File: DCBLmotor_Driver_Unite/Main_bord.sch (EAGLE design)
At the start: 50 parts, among them CN1 DF11-16DP-2DSA, CN2 DF11-16DP-2DSA, CN3 DF11-4DS-2C, CN4 HIF3FC-10PA-2.54DSA(71), CN5 HIF3FC-10PA-2.54DSA(71), IC1 TMPM370FYFG, IC2 MCP2561FD-E/MF, IC3 AM26C32CD, IC4 AM26C32CD, SW1 CVS-02TB

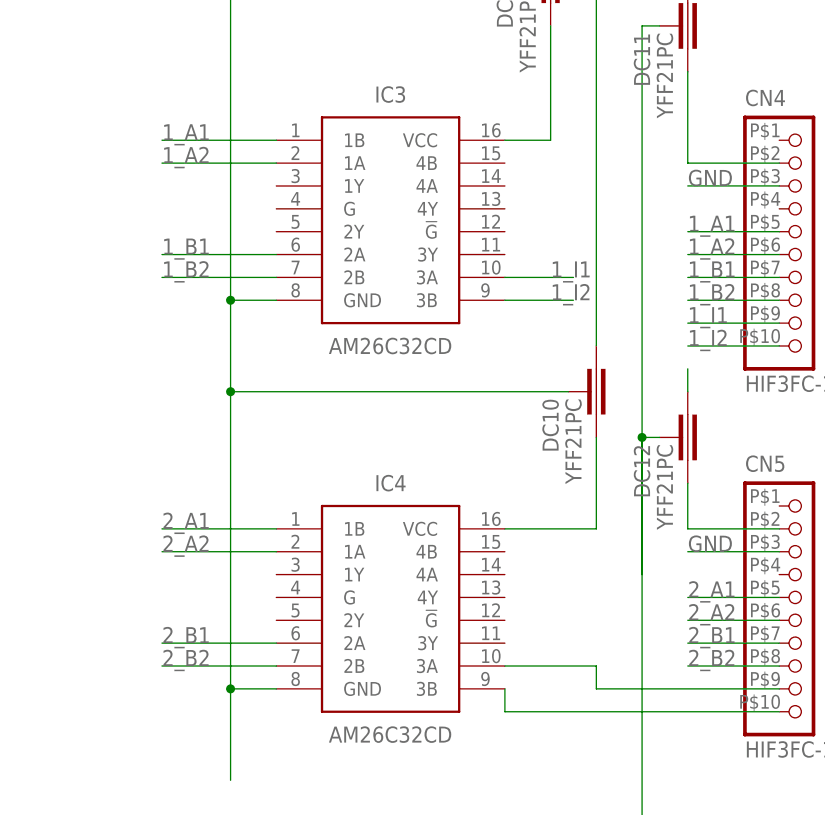
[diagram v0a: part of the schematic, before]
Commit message: Mount Endcoder
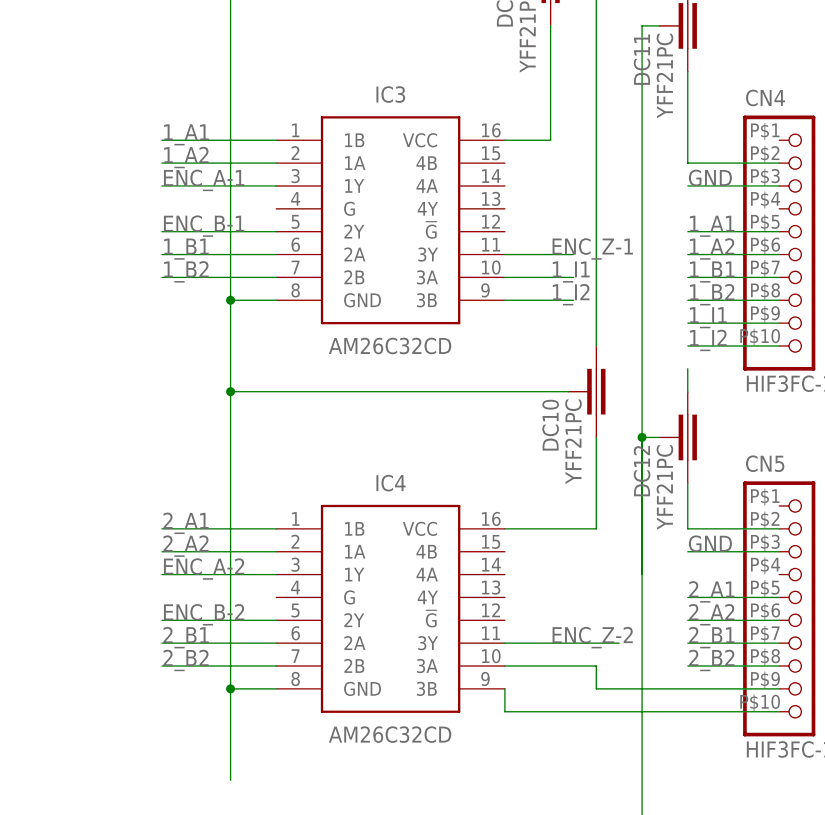
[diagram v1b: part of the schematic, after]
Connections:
- net ENC_A-1: now also IC3.1Y
- net ENC_A-2: now also IC4.1Y
- net ENC_B-1: now also IC3.2Y
- net ENC_B-2: now also IC4.2Y
- net ENC_Z-1: now also IC3.3Y
- net ENC_Z-2: now also IC4.3Y
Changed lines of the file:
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@@
 <label x="38.1" y="-20.32" size="1.778" layer="95" rot="R90"/>
+</segment>
+<segment>
+<wire x1="-83.82" y1="-53.34" x2="-91.44" y2="-53.34" width="0.1524" layer="91"/>
+<label x="-86.36" y="-53.34" size="1.778" layer="95"/>
+<pinref part="IC3" gate="G$1" pin="3Y"/>
 </segment>
 </net>
@@
 <label x="114.3" y="17.78" size="1.778" layer="95"/>
 </segment>
+<segment>
+<wire x1="-129.54" y1="-88.9" x2="-116.84" y2="-88.9" width="0.1524" layer="91"/>
+<label x="-129.54" y="-88.9" size="1.778" layer="95"/>
+<pinref part="IC4" gate="G$1" pin="1Y"/>
+</segment>
 </net>
 <net name="ENC_B-2" class="0">
@@
 <wire x1="111.76" y1="20.32" x2="121.92" y2="20.32" width="0.1524" layer="91"/>
 <label x="114.3" y="20.32" size="1.778" layer="95"/>
+</segment>
+<segment>
+<wire x1="-129.54" y1="-93.98" x2="-116.84" y2="-93.98" width="0.1524" layer="91"/>
+<label x="-129.54" y="-93.98" size="1.778" layer="95"/>
+<pinref part="IC4" gate="G$1" pin="2Y"/>
 </segment>
 </net>
@@
 <label x="114.3" y="22.86" size="1.778" layer="95"/>
 </segment>
+<segment>
+<wire x1="-91.44" y1="-96.52" x2="-78.74" y2="-96.52" width="0.1524" layer="91"/>
+<label x="-86.36" y="-96.52" size="1.778" layer="95"/>
+<pinref part="IC4" gate="G$1" pin="3Y"/>
+</segment>
 </net>
 <net name="ENC_B-1" class="0">
@@
 <wire x1="35.56" y1="-7.62" x2="35.56" y2="-20.32" width="0.1524" layer="91"/>
 <label x="35.56" y="-20.32" size="1.778" layer="95" rot="R90"/>
+</segment>
+<segment>
+<wire x1="-116.84" y1="-50.8" x2="-129.54" y2="-50.8" width="0.1524" layer="91"/>
+<label x="-129.54" y="-50.8" size="1.778" layer="95"/>
+<pinref part="IC3" gate="G$1" pin="2Y"/>
 </segment>
 </net>
@@
 <label x="33.02" y="-20.32" size="1.778" layer="95" rot="R90"/>
 </segment>
+<segment>
+<wire x1="-116.84" y1="-45.72" x2="-129.54" y2="-45.72" width="0.1524" layer="91"/>
+<label x="-129.54" y="-45.72" size="1.778" layer="95"/>
+<pinref part="IC3" gate="G$1" pin="1Y"/>
+</segment>
 </net>

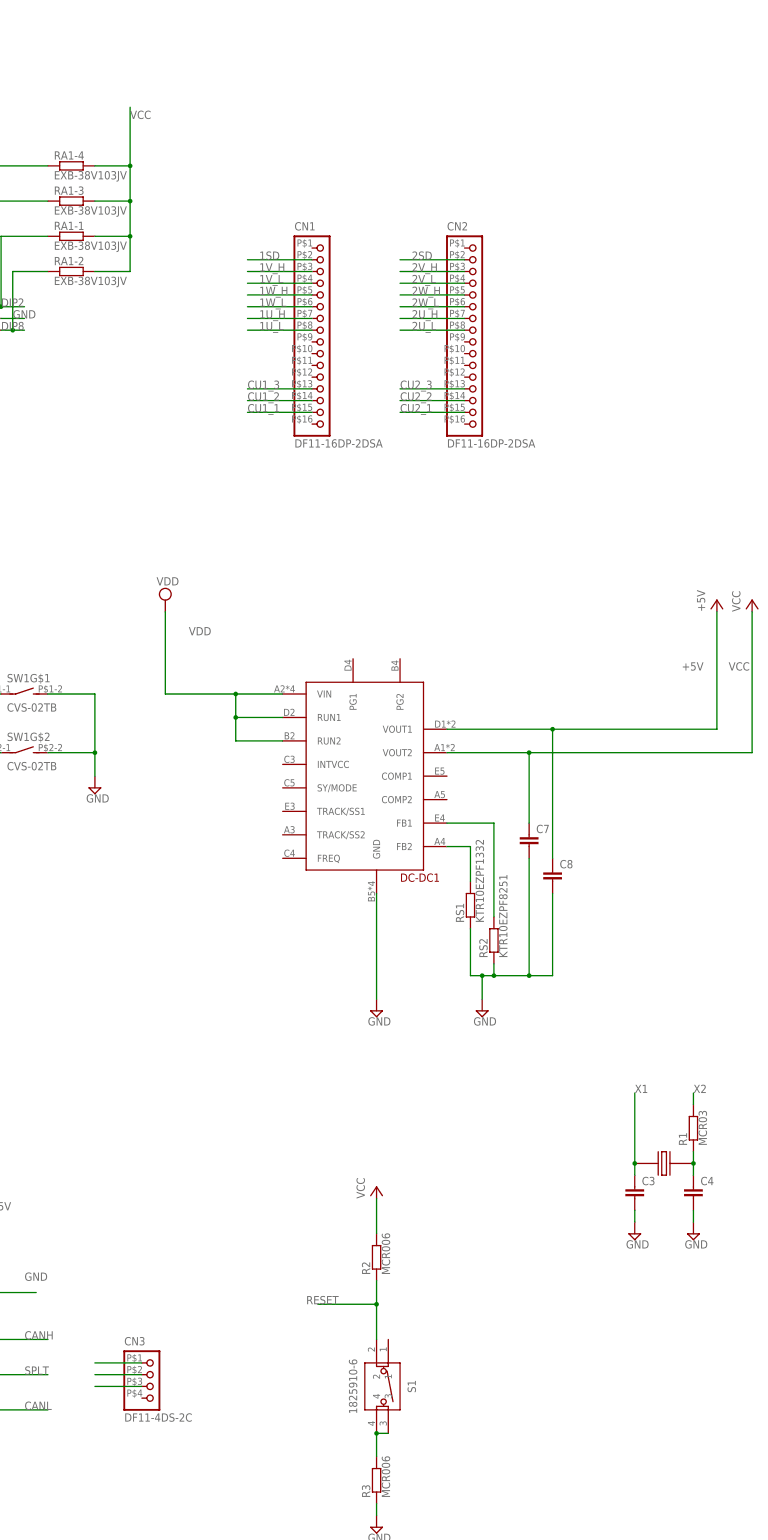
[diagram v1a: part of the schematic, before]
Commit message: Mount new parts
mount 
holl conecter
change
reset switch
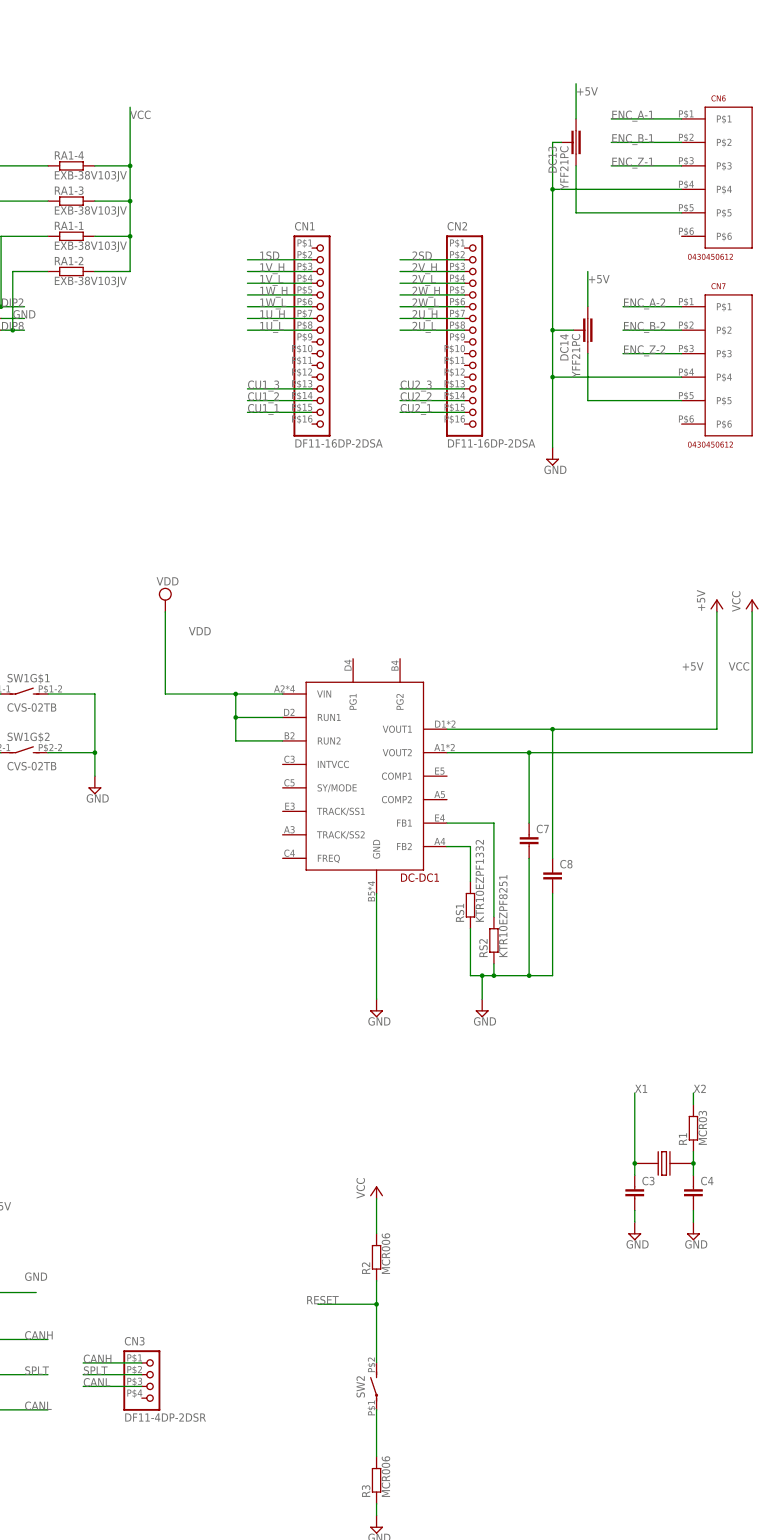
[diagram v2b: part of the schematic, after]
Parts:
- removed S1: 1825910-6, 1825910-6:1825910-6
- added CN6, CN7: 0430450612, Molex:0430450612
- added DC13, DC14: YFF21PC, TDK:YFF21PC
- added SW2: EVQ-PE104K, Panasonic:EVQ-PE104K
- CN3: value DF11-4DS-2C -> DF11-4DP-2DSR; device Hirose:DF11-4DS-2C -> Hirose:DF11-4DP-2DSR
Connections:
- new net N$32: CN6.P$5, DC13.P$2
- new net N$33: CN7.P$5, DC14.P$2
- net +5V: now also DC13.P$1, DC14.P$1
- net ENC_A-1: now also CN6.P$1
- net ENC_A-2: now also CN7.P$1
- net ENC_B-1: now also CN6.P$2
- net ENC_B-2: now also CN7.P$2
- net ENC_Z-1: now also CN6.P$3
- net ENC_Z-2: now also CN7.P$3
- net GND: now also CN6.P$4, CN7.P$4, DC13.GND, DC14.GND
- net N$12: now also SW2.P; no longer S1.3, S1.4
- net RESET: now also SW2.S; no longer S1.2
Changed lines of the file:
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@@
 <part name="R3" library="ROHM" deviceset="MCR006" device=""/>
 <part name="SUPPLY15" library="supply2" library_urn="urn:adsk.eagle:library:372" deviceset="GND" device=""/>
-<part name="S1" library="1825910-6" deviceset="1825910-6" device=""/>
 <part name="P+2" library="supply1" library_urn="urn:adsk.eagle:library:371" deviceset="VCC" device="" value="+5V"/>
 <part name="P+3" library="supply1" library_urn="urn:adsk.eagle:library:371" deviceset="VCC" device="" value="+5V"/>
@@
 <part name="R4" library="ROHM" deviceset="MCR006" device=""/>
 <part name="R5" library="ROHM" deviceset="MCR006" device=""/>
-<part name="CN3" library="Hirose" deviceset="DF11-4DS-2C" device=""/>
+<part name="CN3" library="Hirose" deviceset="DF11-4DP-2DSR" device=""/>
 <part name="S2" library="220AMA16R" deviceset="220AMA16R" device=""/>
 <part name="SW1" library="Nidec" deviceset="CVS-02TB" device=""/>
@@
 <part name="DC11" library="TDK" deviceset="YFF21PC" device=""/>
 <part name="DC12" library="TDK" deviceset="YFF21PC" device=""/>
+<part name="SW2" library="Panasonic" deviceset="EVQ-PE104K" device=""/>
+<part name="CN6" library="Molex" deviceset="0430450612" device=""/>
+<part name="CN7" library="Molex" deviceset="0430450612" device=""/>
+<part name="DC13" library="TDK" deviceset="YFF21PC" device=""/>
+<part name="DC14" library="TDK" deviceset="YFF21PC" device=""/>
+<part name="SUPPLY17" library="supply2" library_urn="urn:adsk.eagle:library:372" deviceset="GND" device=""/>
 </parts>
 <sheets>
@@
 <instance part="R3" gate="G$1" x="393.7" y="-119.38" rot="R90"/>
 <instance part="SUPPLY15" gate="GND" x="393.7" y="-129.54"/>
-<instance part="S1" gate="G$1" x="396.24" y="-88.9" rot="R270"/>
 <instance part="P+2" gate="VCC" x="246.38" y="81.28"/>
 <instance part="P+3" gate="VCC" x="231.14" y="81.28"/>
@@
 <instance part="DC11" gate="G$1" x="-71.12" y="-27.94" rot="R270"/>
 <instance part="DC12" gate="G$1" x="-71.12" y="-73.66" rot="R270"/>
+<instance part="SW2" gate="G$1" x="393.7" y="-99.06"/>
+<instance part="CN6" gate="G$1" x="464.82" y="165.1"/>
+<instance part="CN7" gate="G$1" x="464.82" y="124.46"/>
+<instance part="DC13" gate="G$1" x="436.88" y="170.18" rot="R270"/>
+<instance part="DC14" gate="G$1" x="439.42" y="129.54" rot="R270"/>
+<instance part="SUPPLY17" gate="GND" x="431.8" y="101.6"/>
 </instances>
 <busses>
@@
 <wire x1="-76.2" y1="-73.66" x2="-76.2" y2="-116.84" width="0.1524" layer="91"/>
 </segment>
+<segment>
+<pinref part="DC13" gate="G$1" pin="GND"/>
+<wire x1="433.76" y1="170.18" x2="431.8" y2="170.18" width="0.1524" layer="91"/>
+<wire x1="431.8" y1="170.18" x2="431.8" y2="160.02" width="0.1524" layer="91"/>
+<pinref part="DC14" gate="G$1" pin="GND"/>
+<wire x1="431.8" y1="160.02" x2="431.8" y2="129.54" width="0.1524" layer="91"/>
+<wire x1="431.8" y1="129.54" x2="431.8" y2="119.38" width="0.1524" layer="91"/>
+<wire x1="431.8" y1="119.38" x2="431.8" y2="104.14" width="0.1524" layer="91"/>
+<wire x1="436.3" y1="129.54" x2="431.8" y2="129.54" width="0.1524" layer="91"/>
+<junction x="431.8" y="129.54"/>
+<pinref part="CN7" gate="G$1" pin="P$4"/>
+<wire x1="459.74" y1="119.38" x2="431.8" y2="119.38" width="0.1524" layer="91"/>
+<junction x="431.8" y="119.38"/>
+<pinref part="CN6" gate="G$1" pin="P$4"/>
+<wire x1="459.74" y1="160.02" x2="431.8" y2="160.02" width="0.1524" layer="91"/>
+<junction x="431.8" y="160.02"/>
+<pinref part="SUPPLY17" gate="GND" pin="GND"/>
+</segment>
 </net>
 <net name="N$7" class="0">
@@
 <wire x1="-71.12" y1="-68.58" x2="-71.12" y2="-66.04" width="0.1524" layer="91"/>
 </segment>
+<segment>
+<pinref part="DC13" gate="G$1" pin="P$1"/>
+<wire x1="436.88" y1="175.26" x2="436.88" y2="182.88" width="0.1524" layer="91"/>
+<label x="436.88" y="180.34" size="1.778" layer="95"/>
+</segment>
+<segment>
+<pinref part="DC14" gate="G$1" pin="P$1"/>
+<wire x1="439.42" y1="134.62" x2="439.42" y2="142.24" width="0.1524" layer="91"/>
+<label x="439.42" y="139.7" size="1.778" layer="95"/>
+</segment>
 </net>
 <net name="VDD" class="0">
@@
 <junction x="393.7" y="-81.28"/>
 <label x="378.46" y="-81.28" size="1.778" layer="95"/>
-<pinref part="S1" gate="G$1" pin="2"/>
-<wire x1="393.7" y1="-88.9" x2="393.7" y2="-81.28" width="0.1524" layer="91"/>
+<wire x1="393.7" y1="-93.98" x2="393.7" y2="-81.28" width="0.1524" layer="91"/>
+<pinref part="SW2" gate="G$1" pin="S"/>
 </segment>
 </net>
@@
 <segment>
 <pinref part="R3" gate="G$1" pin="1"/>
-<pinref part="S1" gate="G$1" pin="4"/>
-<wire x1="393.7" y1="-114.3" x2="393.7" y2="-109.22" width="0.1524" layer="91"/>
-<pinref part="S1" gate="G$1" pin="3"/>
-<wire x1="393.7" y1="-109.22" x2="396.24" y2="-109.22" width="0.1524" layer="91"/>
-<junction x="393.7" y="-109.22"/>
+<pinref part="SW2" gate="G$1" pin="P"/>
+<wire x1="393.7" y1="-104.14" x2="393.7" y2="-114.3" width="0.1524" layer="91"/>
 </segment>
 </net>
@@
 <pinref part="IC3" gate="G$1" pin="3Y"/>
 </segment>
+<segment>
+<wire x1="459.74" y1="165.1" x2="444.5" y2="165.1" width="0.1524" layer="91"/>
+<label x="444.5" y="165.1" size="1.778" layer="95"/>
+<pinref part="CN6" gate="G$1" pin="P$3"/>
+</segment>
 </net>
 <net name="ENC_A-2" class="0">
@@
 <pinref part="IC4" gate="G$1" pin="1Y"/>
 </segment>
+<segment>
+<wire x1="447.04" y1="134.62" x2="459.74" y2="134.62" width="0.1524" layer="91"/>
+<label x="447.04" y="134.62" size="1.778" layer="95"/>
+<pinref part="CN7" gate="G$1" pin="P$1"/>
+</segment>
 </net>
 <net name="ENC_B-2" class="0">
@@
 <pinref part="IC4" gate="G$1" pin="2Y"/>
 </segment>
+<segment>
+<wire x1="447.04" y1="129.54" x2="459.74" y2="129.54" width="0.1524" layer="91"/>
+<label x="447.04" y="129.54" size="1.778" layer="95"/>
+<pinref part="CN7" gate="G$1" pin="P$2"/>
+</segment>
 </net>
 <net name="ENC_Z-2" class="0">
@@
 <pinref part="IC4" gate="G$1" pin="3Y"/>
 </segment>
+<segment>
+<wire x1="447.04" y1="124.46" x2="459.74" y2="124.46" width="0.1524" layer="91"/>
+<label x="447.04" y="124.46" size="1.778" layer="95"/>
+<pinref part="CN7" gate="G$1" pin="P$3"/>
+</segment>
 </net>
 <net name="ENC_B-1" class="0">
@@
 <pinref part="IC3" gate="G$1" pin="2Y"/>
 </segment>
+<segment>
+<wire x1="459.74" y1="170.18" x2="444.5" y2="170.18" width="0.1524" layer="91"/>
+<label x="444.5" y="170.18" size="1.778" layer="95"/>
+<pinref part="CN6" gate="G$1" pin="P$2"/>
+</segment>
 </net>
 <net name="ENC_A-1" class="0">
@@
 <label x="-129.54" y="-45.72" size="1.778" layer="95"/>
 <pinref part="IC3" gate="G$1" pin="1Y"/>
+</segment>
+<segment>
+<wire x1="459.74" y1="175.26" x2="444.5" y2="175.26" width="0.1524" layer="91"/>
+<label x="444.5" y="175.26" size="1.778" layer="95"/>
+<pinref part="CN6" gate="G$1" pin="P$1"/>
 </segment>
 </net>
@@
 <segment>
 <pinref part="CN3" gate="G$1" pin="1"/>
-<wire x1="342.9" y1="-93.98" x2="332.74" y2="-93.98" width="0.1524" layer="91"/>
+<wire x1="342.9" y1="-93.98" x2="330.2" y2="-93.98" width="0.1524" layer="91"/>
+<label x="330.2" y="-93.98" size="1.778" layer="95"/>
 </segment>
 </net>
@@
 <segment>
 <pinref part="CN3" gate="G$1" pin="3"/>
-<wire x1="342.9" y1="-99.06" x2="332.74" y2="-99.06" width="0.1524" layer="91"/>
+<wire x1="342.9" y1="-99.06" x2="330.2" y2="-99.06" width="0.1524" layer="91"/>
+<label x="330.2" y="-99.06" size="1.778" layer="95"/>
 </segment>
 </net>
@@
 <segment>
 <pinref part="CN3" gate="G$1" pin="2"/>
-<wire x1="342.9" y1="-96.52" x2="332.74" y2="-96.52" width="0.1524" layer="91"/>
+<wire x1="342.9" y1="-96.52" x2="330.2" y2="-96.52" width="0.1524" layer="91"/>
+<label x="330.2" y="-96.52" size="1.778" layer="95"/>
 </segment>
 </net>
@@
 </segment>
 </net>
+<net name="N$32" class="0">
+<segment>
+<pinref part="DC13" gate="G$1" pin="P$2"/>
+<pinref part="CN6" gate="G$1" pin="P$5"/>
+<wire x1="436.88" y1="165.1" x2="436.88" y2="154.94" width="0.1524" layer="91"/>
+<wire x1="436.88" y1="154.94" x2="459.74" y2="154.94" width="0.1524" layer="91"/>
+</segment>
+</net>
+<net name="N$33" class="0">
+<segment>
+<pinref part="DC14" gate="G$1" pin="P$2"/>
+<pinref part="CN7" gate="G$1" pin="P$5"/>
+<wire x1="439.42" y1="124.46" x2="439.42" y2="114.3" width="0.1524" layer="91"/>
+<wire x1="439.42" y1="114.3" x2="459.74" y2="114.3" width="0.1524" layer="91"/>
+</segment>
+</net>

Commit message: Version1 per finshed
Per complete Version1
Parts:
- added 0R1, 0R2: 5106, Keystone:5106
- added C5: T356L107K016AT, KEMET:T356L107K016AT
- added CN10: (no value), jst-xh:B2B-XH-A
- added CN8: BM11B-SRSS-TB, JST:BM11B-SRSS-TB
- added CN9: (no value), jst-xh:B4B-XH-A
- added CR10, CR11, CR12, CR5, CR6, CR7, CR8: NSI50010YT1G, ON Semiconductor:NSI50010YT1G
- added DC15: YFF15PC1C104MT000N, TDK:YFF15PC1C104MT000N
- added IC5: LTC2862A, LT:LTC2862A
- added LED1, LED2: CL-340T-SD-T, Citizen:CL-340T-SD-T
- added LED3: CL-196YG-CD-T, Citizen:CL-196YG-CD-T
- added R8: MCR006, ROHM:MCR006
- DC6, DC7, DC8: value YFF21PC -> YFF15PC1C104MT000N; device TDK:YFF21PC -> TDK:YFF15PC1C104MT000N
- renumbered XTAL2 to XTAL1
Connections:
- new net A*: CN9.3, IC5.A*, R8.2
- new net B*: CN9.4, IC5.B*, R8.1
- new net LED1_1: CR6.P$C, IC1.CTS0/SCLK0/PE2
- new net LED1_2: CR12.P$C, IC1.TB4OUT/PE3
- new net LED1_3: CR7.P$C, IC1.INT5/TB2IN/PE4
- new net LED2_1: CR10.P$C, IC1.TB2OUT/PE5
- new net LED2_2: CR11.P$C, IC1.INT6/TB3IN/PE6
- new net LED2_3: CR8.P$C, IC1.INT7/TB3OUT/PE7
- new net N$34: CR5.P$A, LED3.C
- new net N$37: CR7.P$A, LED1.B_C
- new net N$38: CR12.P$A, LED1.R_C
- new net N$39: CR6.P$A, LED1.G_C
- new net N$40: CR8.P$A, LED2.B_C
- new net N$41: CR11.P$A, LED2.R_C
- new net N$42: CR10.P$A, LED2.G_C
- new net N$43: DC15.P$1, IC5.VCC
- new net N$44: 0R2.1, CN9.2
- new net N$46: 0R1.1, CN9.1
- net +5V: now also 0R2.2, DC15.P$2
- net GND: now also 0R1.2, C5.2, CN10.2, CR5.P$C, DC15.GND, IC5.GND
- net N$18: now also CN8.P$5
- net N$19: now also CN8.P$6
- net N$20: now also CN8.P$9
- net N$21: now also CN8.P$7
- net N$22: now also CN8.P$8
- net N$23: now also CN8.P$4
- net N$24: now also CN8.P$3
- net N$25: now also CN8.P$2
- net RESET: now also CN8.P$10
- net RX0: now also IC5.DI
- net TX0: now also IC5.RO
- net VCC: now also CN8.P$1, LED1.A_G, LED1.B_A, LED1.R_A, LED2.A_G, LED2.B_A, LED2.R_A, LED3.A
- net VDD: now also C5.+, CN10.1

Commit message: Assigned Parts No.
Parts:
- removed R3: MCR006, ROHM:MCR006
- DC1, DC10, DC11, DC12, DC13, DC14, DC2, DC3, DC4, DC5, DC9: value YFF21PC -> YFF21PC1E104MT000N; device TDK:YFF21PC -> TDK:YFF21PC1E104MT000N
- R2: value MCR006 -> CRCW06031K00JNEAC; device ROHM:MCR006 -> VISHAY:CRCW06031K00JNEAC
- R4, R5: value MCR006 -> CRCW060360R4FKEA; device ROHM:MCR006 -> VISHAY:CRCW060360R4FKEA
- R6, R7: value MCR03 -> CRCW06031K00JNEAC; device ROHM:MCR03 -> VISHAY:CRCW06031K00JNEAC
- R8: value MCR006 -> CRCW0603100RJNEAC; device ROHM:MCR006 -> VISHAY:CRCW0603100RJNEAC
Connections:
- removed net N$12: R3.1, SW2.P
- new net RS_DIR: IC1.TB6IN/RXD1/PA6, IC5.DE, IC5.RE
- net +5V: now also CN8.P$1, LED1.A_G, LED1.B_A, LED1.R_A, LED2.A_G, LED2.B_A, LED2.R_A, LED3.A, R6.1, R7.1, RA1-1.1, RA1-2.1, RA1-3.1, RA1-4.1
- net GND: now also SW2.P; no longer R3.2
- net VCC: no longer CN8.P$1, LED1.A_G, LED1.B_A, LED1.R_A, LED2.A_G, LED2.B_A, LED2.R_A, LED3.A, R6.1, R7.1, RA1-1.1, RA1-2.1, RA1-3.1, RA1-4.1
